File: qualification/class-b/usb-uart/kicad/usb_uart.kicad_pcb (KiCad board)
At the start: 4 copper layers, 50.4 x 38.3 mm, 40 parts, among them J1 12401610E4#2A, J2 UART1, J3 FLOW1, J4 RS485, U1 CH342F, U2 LDO, U3 THVD1450D

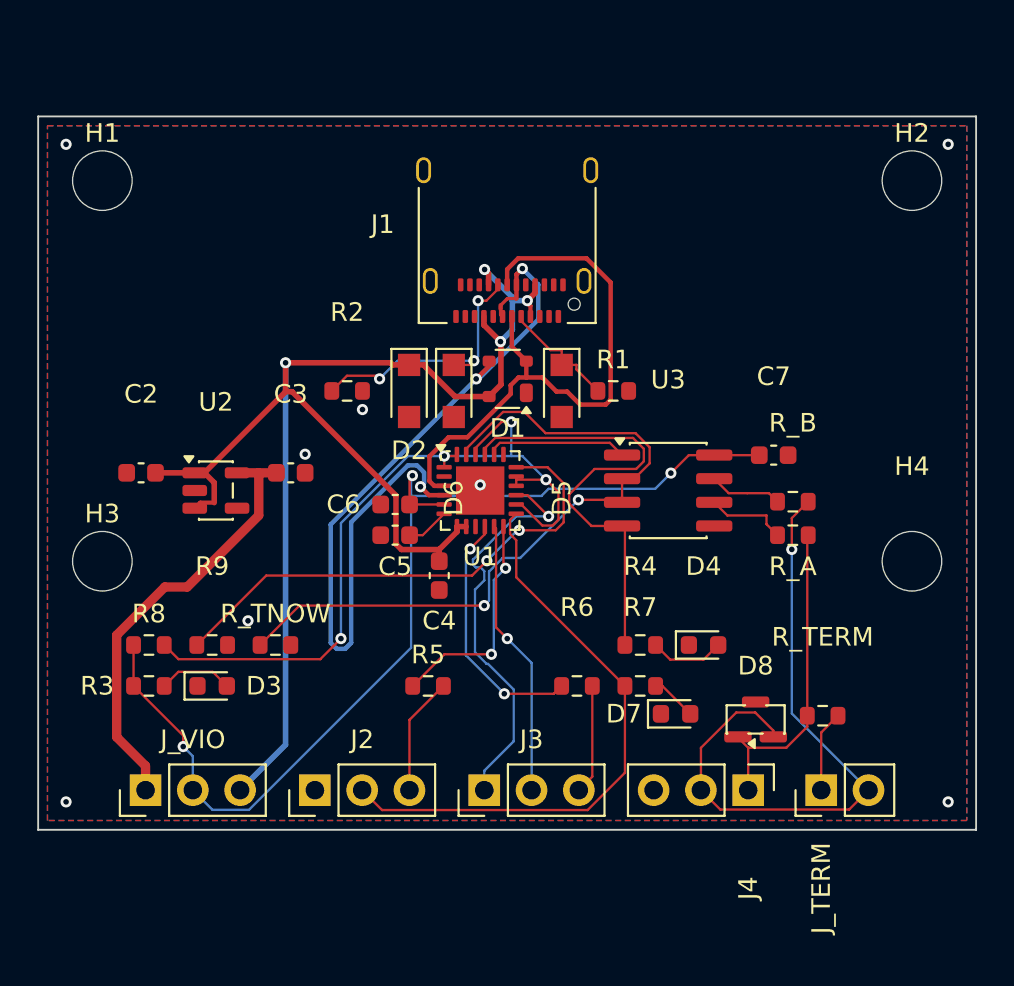
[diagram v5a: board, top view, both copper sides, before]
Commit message: SYN-66 - Route the board again with ground vias, screw-head keepouts and TX LEDs on data
Route the board with the four integrated tool PRs (#154, #162, #175, #176). Every outer SMD ground pad now has a ground via within 2 mm, the corner vias are clear of the M3 holes, and the result is 0 open nets, KiCad DRC 0 errors, release gate passed.

The TX LEDs now run from VIO into TXD0 and TXD1, so they light only while data goes out. USB path lengths per connector contact, the ground tie table, the 134 ERC warnings and the unconfirmed J1 oval hole and via annular ring questions are in the README and QUALIFICATION.md. New pictures, STEP and SHA256SUMS match the delivered board.

Signed-off-by: nyagamunene <stevenyaga2014@gmail.com>
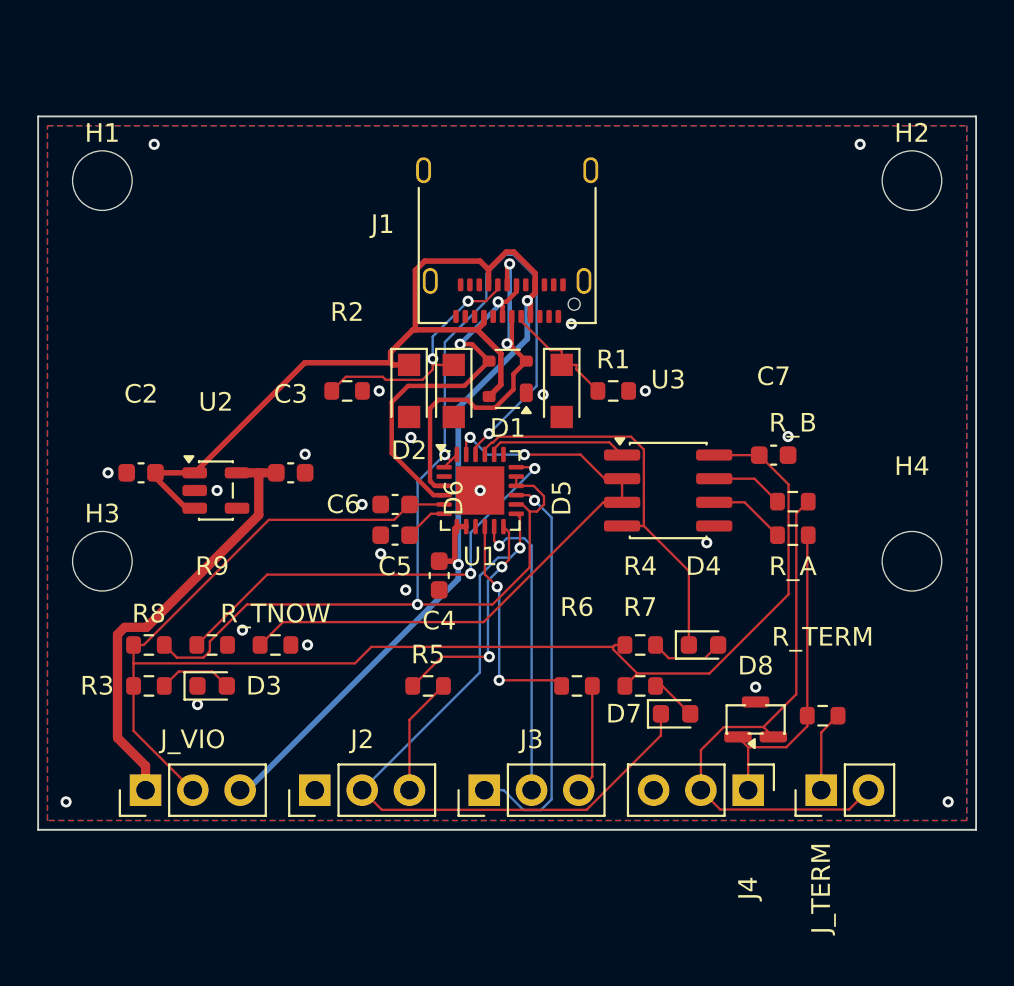
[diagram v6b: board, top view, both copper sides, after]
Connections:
- D4 pad 1: GND -> TXD0
- D7 pad 1: GND -> TXD1
- R4 pad 1: TXD0 -> VIO
- R7 pad 1: TXD1 -> VIO
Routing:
- net USB_DN: track 45.3 -> 20.2 mm, vias 3 -> 2
- net MODEM_IDLE: track 42.9 -> 64.9 mm, vias 4 -> 3
- net VIO: track 57.3 -> 79.1 mm, vias 3 -> 0
- net USB_DP: track 31.8 -> 20.3 mm, vias 0 -> 2
- net TXD1: track 32.0 -> 38.1 mm, vias 0 -> 1
- net RS485_B_BUS: track 35.1 -> 29.7 mm, vias 1 -> 0
- net TNOW0: track 39.3 -> 34.0 mm
- net CTS0_LOW: track 27.4 -> 24.4 mm
- net TXD0: track 25.1 -> 22.1 mm
- net VBUS: track 78.5 -> 80.8 mm, vias 4 -> 2
- net CTS1_MCU: track 13.5 -> 12.1 mm
- net RTS1: track 15.0 -> 16.4 mm
- net CC2: track 14.5 -> 13.7 mm, vias 3 -> 2
- net GND: vias 8 -> 22
